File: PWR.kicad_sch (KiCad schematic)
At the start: 32 parts, among them J1 Conn_01x02_Pin, U2 XC6206P332MR, U4 MCP6001-OT, U5 AMS1117-3.3, U6 XL1509-5.0

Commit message: feat: начал работу над проектом пульта управления, продумана входная цепь питания устройства
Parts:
- removed C10, C11: 100u, Capacitor_SMD:C_Elec_6.3x7.7, symbol Device:C_Small_US
- removed C43, C44, C9: 0.1u, Capacitor_SMD:C_0805_2012Metric_Pad1.18x1.45mm_HandSolder, symbol Device:C_Small
- removed D1: SMAJ30CA, Diode_SMD:D_SMA, symbol Diode:SMAJ30CA
- removed D2, D3: SS36, Diode_SMD:D_SMA, symbol Diode:SS36
- removed J1: Conn_01x02_Pin, Connector_PinHeader_2.54mm:PinHeader_1x02_P2.54mm_Vertical, symbol Connector:Conn_01x02_Pin
- removed L4: 47uH, Inductor_SMD:L_12x12mm_H8mm, symbol Inductors:L
- removed L5: BLM21PG121SN1D, Inductor_SMD:L_0805_2012Metric_Pad1.05x1.20mm_HandSolder, symbol Inductors:L
- removed U6: XL1509-5.0, Package_SO:SOIC-8-1EP_3.9x4.9mm_P1.27mm_EP2.29x3mm_ThermalVias, symbol Power_suply:XL1509-5.0
- added C12: 100u, Capacitor_SMD:C_Elec_6.3x7.7, symbol Device:C_Small_US
- added D1: SS32, Diode_SMD:D_SMA, symbol Diode:SS32
- added D3: SMAJ5.0CA, Diode_SMD:D_SMA, symbol Diode:SMAJ5.0CA
- added J1: USB_B_Micro, Connector_USB:USB_Micro-B_Wuerth_629105150521, symbol Connector:USB_B_Micro
- R10: value 1k -> 10k
- R9: value 3k -> 10k
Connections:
- net +5V: now also C4.1, L3.2, C12.1
- net GND: now also C12.2, D3.1 (A1), J1.5 (GND)
- net at C34.1, L3.1: now also D1.1 (K)
- removed net +12V: C4.1, L3.2, R9.1
- net +12V_1: no longer names the net of F1.1 (A1)
- net +12V_1: now also J1.1 (VBUS)
- net +12V_in renamed +5V_in
- net +5V_in: now also D1.2 (A), D3.2 (A2)
- new net BAT+: R9.1
- new net Earth: J1.SH (Shield)
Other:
- moved on the sheet: C1, C2, C29, C3, C30, C34, C4, C5, C6, C7, C8, F1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

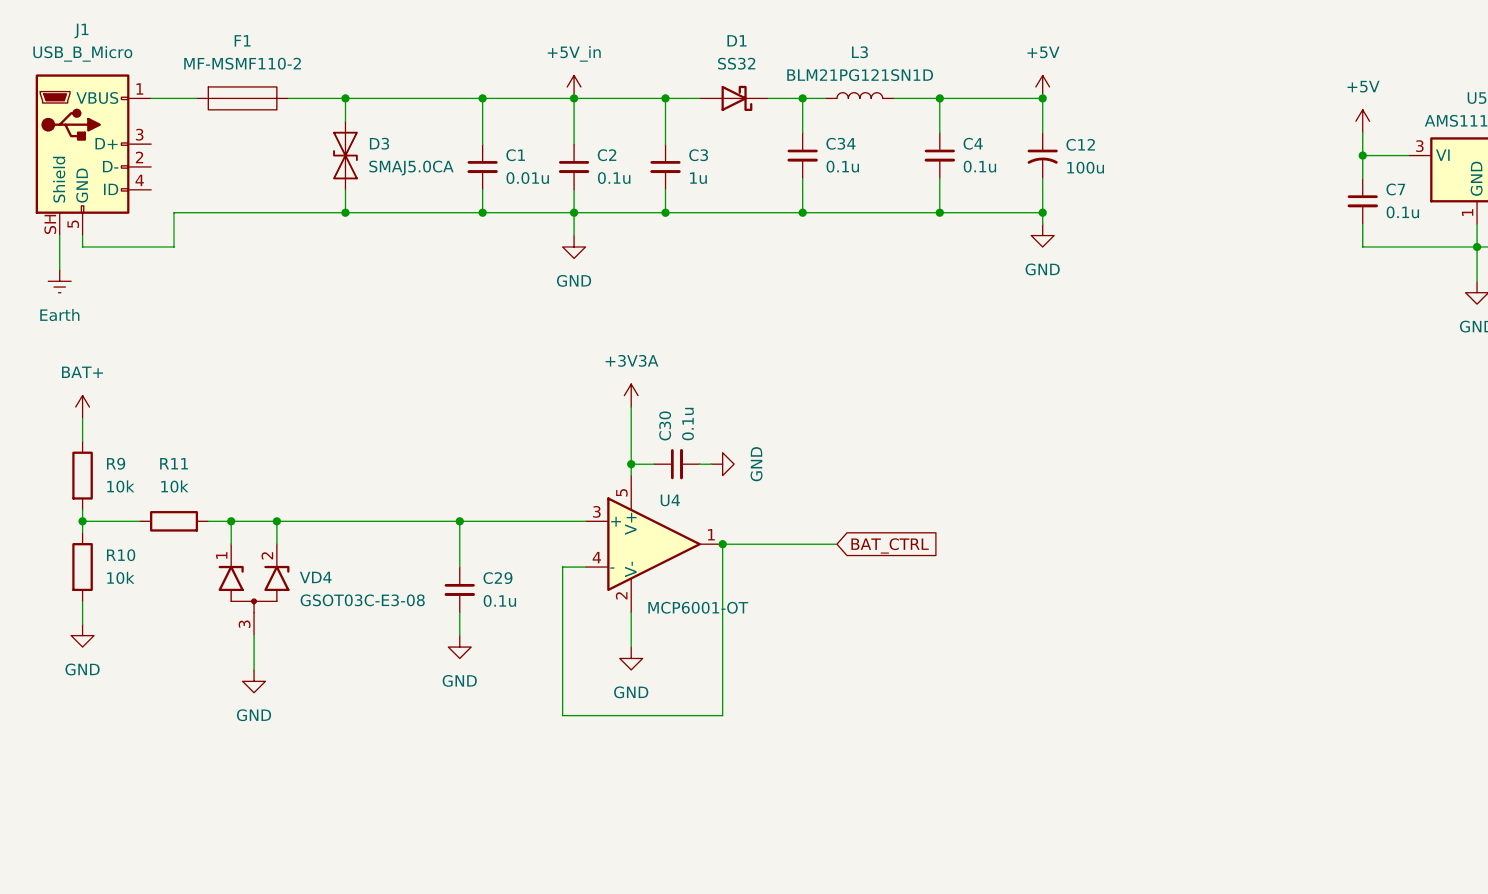
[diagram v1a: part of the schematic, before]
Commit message: feat: добавлен верный разъём USB
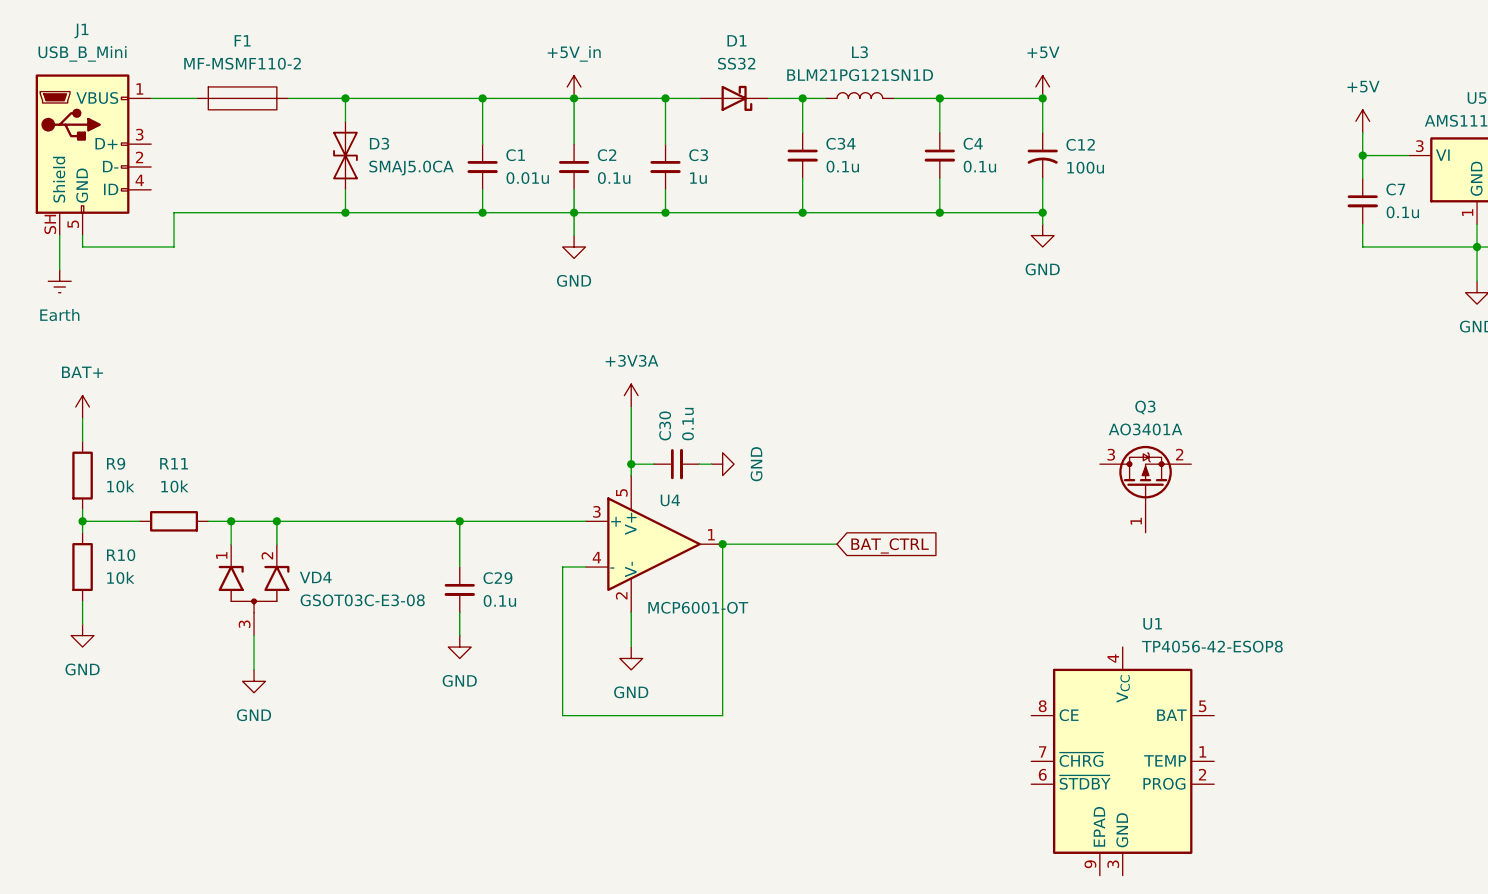
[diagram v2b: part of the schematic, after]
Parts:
- removed J1: USB_B_Micro, Connector_USB:USB_Micro-B_Wuerth_629105150521, symbol Connector:USB_B_Micro
- added J1: USB_B_Mini, Connector_USB:USB_Mini-B_Lumberg_2486_01_Horizontal, symbol Connector:USB_B_Mini
- added Q3: AO3401A, Package_TO_SOT_SMD:SOT-23, symbol Transistor_FET:AO3401A
- added U1: TP4056-42-ESOP8, Package_SO:SOIC-8-1EP_3.9x4.9mm_P1.27mm_EP2.41x3.3mm_ThermalVias, symbol Battery_Management:TP4056-42-ESOP8
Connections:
- net Earth: now also J1.SH (Shield)
- net GND: now also J1.5 (GND)
- net at F1.1 (A1): now also J1.1 (VBUS)
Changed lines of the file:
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@@
-	)
-	(symbol
-		(lib_id "Connector:USB_B_Micro")
-		(at 31.75 54.61 0)
-		(unit 1)
-		(body_style 1)
-		(exclude_from_sim no)
-		(in_bom yes)
-		(on_board yes)
-		(in_pos_files yes)
-		(dnp no)
-		(fields_autoplaced yes)
-		(property "Reference" "J1"
-			(at 31.75 41.91 0)
-			(show_name no)
-			(do_not_autoplace no)
-			(effects
-				(font
-					(size 1.27 1.27)
-				)
-			)
-		)
-		(property "Value" "USB_B_Micro"
-			(at 31.75 44.45 0)
-			(show_name no)
-			(do_not_autoplace no)
-			(effects
-				(font
-					(size 1.27 1.27)
-				)
-			)
-		)
-		(property "Footprint" "Connector_USB:USB_Micro-B_Wuerth_629105150521"
-			(at 35.56 55.88 0)
-			(hide yes)
-			(show_name no)
-			(do_not_autoplace no)
-			(effects
-				(font
-					(size 1.27 1.27)
-				)
-			)
-		)
-		(property "Datasheet" ""
-			(at 35.56 55.88 0)
-			(hide yes)
-			(show_name no)
-			(do_not_autoplace no)
-			(effects
-				(font
-					(size 1.27 1.27)
-				)
-			)
-		)
-		(property "Description" "USB Micro Type B connector"
-			(at 31.75 54.61 0)
-			(hide yes)
-			(show_name no)
-			(do_not_autoplace no)
-			(effects
-				(font
-					(size 1.27 1.27)
-				)
-			)
-		)
-		(pin "1"
-		)
-		(pin "3"
-		)
-		(pin "5"
-		)
-		(pin "2"
-		)
-		(pin "4"
-		)
-		(pin "SH"
-		)
-		(instances
-			(project "Magister_work_v1"
-				(path "/9ff4e5e8-ab59-4c4d-a10a-f8f5e444c5cb/6e6c00e0-c4a8-403b-83b3-c44ac9f0fdda"
-					(reference "J1")
-					(unit 1)
-				)
-			)
-		)
 	)
 	(symbol
@@
 	)
 	(symbol
+		(lib_id "Battery_Management:TP4056-42-ESOP8")
+		(at 147.32 123.19 0)
+		(unit 1)
+		(body_style 1)
+		(exclude_from_sim no)
+		(in_bom yes)
+		(on_board yes)
+		(in_pos_files yes)
+		(dnp no)
+		(fields_autoplaced yes)
+		(property "Reference" "U1"
+			(at 149.4633 107.95 0)
+			(show_name no)
+			(do_not_autoplace no)
+			(effects
+				(font
+					(size 1.27 1.27)
+				)
+				(justify left)
+			)
+		)
+		(property "Value" "TP4056-42-ESOP8"
+			(at 149.4633 110.49 0)
+			(show_name no)
+			(do_not_autoplace no)
+			(effects
+				(font
+					(size 1.27 1.27)
+				)
+				(justify left)
+			)
+		)
+		(property "Footprint" "Package_SO:SOIC-8-1EP_3.9x4.9mm_P1.27mm_EP2.41x3.3mm_ThermalVias"
+			(at 147.828 146.05 0)
+			(hide yes)
+			(show_name no)
+			(do_not_autoplace no)
+			(effects
+				(font
+					(size 1.27 1.27)
+				)
+			)
+		)
+		(property "Datasheet" "https://www.lcsc.com/datasheet/lcsc_datasheet_2410121619_TOPPOWER-Nanjing-Extension-Microelectronics-TP4056-42-ESOP8_C16581.pdf"
+			(at 147.32 148.59 0)
+			(hide yes)
+			(show_name no)
+			(do_not_autoplace no)
+			(effects
+				(font
+					(size 1.27 1.27)
+				)
+			)
+		)
+		(property "Description" "1A Standalone Linear Li-ion/LiPo single-cell battery charger, 4.2V ±1% charge voltage, VCC = 4.0..8.0V, SOIC-8 (SOP-8)"
+			(at 147.828 143.51 0)
+			(hide yes)
+			(show_name no)
+			(do_not_autoplace no)
+			(effects
+				(font
+					(size 1.27 1.27)
+				)
+			)
+		)
+		(pin "4"
+		)
+		(pin "2"
+		)
+		(pin "9"
+		)
+		(pin "1"
+		)
+		(pin "5"
+		)
+		(pin "6"
+		)
+		(pin "8"
+		)
+		(pin "7"
+		)
+		(pin "3"
+		)
+		(instances
+			(project "Magister_work_v1"
+				(path "/9ff4e5e8-ab59-4c4d-a10a-f8f5e444c5cb/6e6c00e0-c4a8-403b-83b3-c44ac9f0fdda"
+					(reference "U1")
+					(unit 1)
+				)
+			)
+		)
+	)
+	(symbol
 		(lib_id "power:GND")
 		(at 138.43 63.5 0)
@@
 	)
 	(symbol
+		(lib_id "Transistor_FET:AO3401A")
+		(at 149.86 92.71 90)
+		(unit 1)
+		(body_style 1)
+		(exclude_from_sim no)
+		(in_bom yes)
+		(on_board yes)
+		(in_pos_files yes)
+		(dnp no)
+		(fields_autoplaced yes)
+		(property "Reference" "Q3"
+			(at 149.86 83.82 90)
+			(show_name no)
+			(do_not_autoplace no)
+			(effects
+				(font
+					(size 1.27 1.27)
+				)
+			)
+		)
+		(property "Value" "AO3401A"
+			(at 149.86 86.36 90)
+			(show_name no)
+			(do_not_autoplace no)
+			(effects
+				(font
+					(size 1.27 1.27)
+				)
+			)
+		)
+		(property "Footprint" "Package_TO_SOT_SMD:SOT-23"
+			(at 151.765 87.63 0)
+			(hide yes)
+			(show_name no)
+			(do_not_autoplace no)
+			(effects
+				(font
+					(size 1.27 1.27)
+					(italic yes)
+				)
+				(justify left)
+			)
+		)
+		(property "Datasheet" "http://www.aosmd.com/pdfs/datasheet/AO3401A.pdf"
+			(at 153.67 87.63 0)
+			(hide yes)
+			(show_name no)
+			(do_not_autoplace no)
+			(effects
+				(font
+					(size 1.27 1.27)
+				)
+				(justify left)
+			)
+		)
+		(property "Description" "-4.0A Id, -30V Vds, P-Channel MOSFET, SOT-23"
+			(at 149.86 92.71 0)
+			(hide yes)
+			(show_name no)
+			(do_not_autoplace no)
+			(effects
+				(font
+					(size 1.27 1.27)
+				)
+			)
+		)
+		(pin "1"
+		)
+		(pin "3"
+		)
+		(pin "2"
+		)
+		(instances
+			(project "Magister_work_v1"
+				(path "/9ff4e5e8-ab59-4c4d-a10a-f8f5e444c5cb/6e6c00e0-c4a8-403b-83b3-c44ac9f0fdda"
+					(reference "Q3")
+					(unit 1)
+				)
+			)
+		)
+	)
+	(symbol
 		(lib_id "Power_suply:XC6206P332MR")
 		(at 227.33 52.07 0)
@@
 					(unit 1)
 				)
+			)
+		)
+	)
+	(symbol
+		(lib_id "Connector:USB_B_Mini")
+		(at 31.75 54.61 0)
+		(unit 1)
+		(body_style 1)
+		(exclude_from_sim no)
+		(in_bom yes)
+		(on_board yes)
+		(in_pos_files yes)
+		(dnp no)
+		(fields_autoplaced yes)
+		(property "Reference" "J1"
+			(at 31.75 41.91 0)
+			(show_name no)
+			(do_not_autoplace no)
+			(effects
+				(font
+					(size 1.27 1.27)
+				)
+			)
+		)
+		(property "Value" "USB_B_Mini"
+			(at 31.75 44.45 0)
+			(show_name no)
+			(do_not_autoplace no)
+			(effects
+				(font
+					(size 1.27 1.27)
+				)
+			)
+		)
+		(property "Footprint" "Connector_USB:USB_Mini-B_Lumberg_2486_01_Horizontal"
+			(at 35.56 55.88 0)
+			(hide yes)
+			(show_name no)
+			(do_not_autoplace no)
+			(effects
+				(font
+					(size 1.27 1.27)
+				)
+			)
+		)
+		(property "Datasheet" ""
+			(at 35.56 55.88 0)
+			(hide yes)
+			(show_name no)
+			(do_not_autoplace no)
+			(effects
+				(font
+					(size 1.27 1.27)
+				)
+			)
+		)
+		(property "Description" "USB Mini Type B connector"
+			(at 31.75 54.61 0)
+			(hide yes)
+			(show_name no)
+			(do_not_autoplace no)
+			(effects
+				(font
+					(size 1.27 1.27)
+				)
+			)
+		)
+		(pin "5"
+		)
+		(pin "4"
+		)
+		(pin "SH"
+		)
+		(pin "1"
+		)
+		(pin "2"
+		)
+		(pin "3"
+		)
+		(instances
+			(project "Magister_work_v1"
+				(path "/9ff4e5e8-ab59-4c4d-a10a-f8f5e444c5cb/6e6c00e0-c4a8-403b-83b3-c44ac9f0fdda"
+					(reference "J1")
+					(unit 1)
+				)

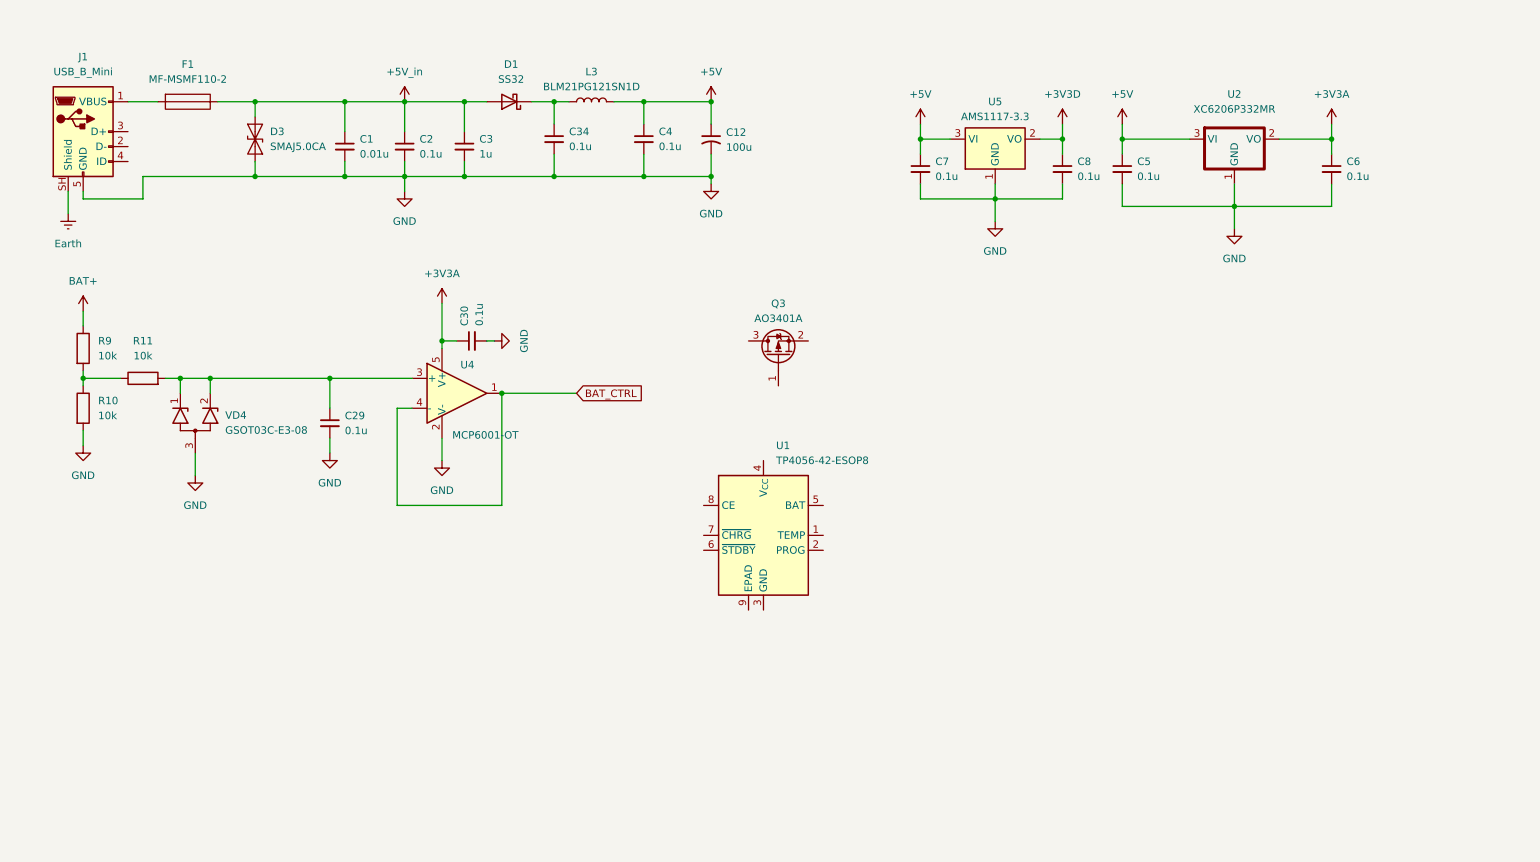
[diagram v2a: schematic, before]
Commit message: feat: добавлена цепь питания и заряда батареи для аварийного питания
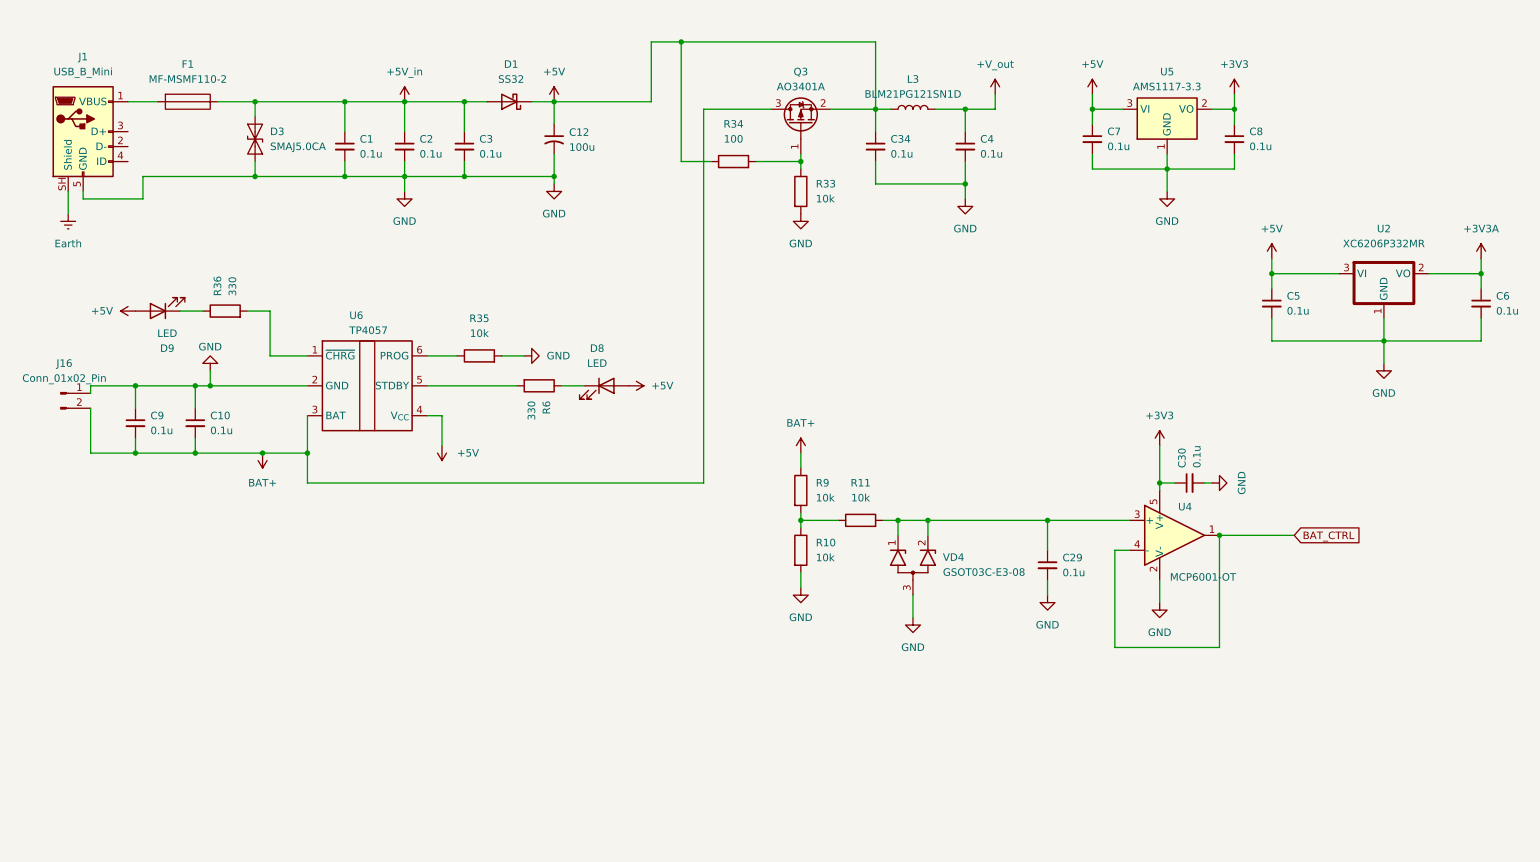
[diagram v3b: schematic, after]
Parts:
- removed U1: TP4056-42-ESOP8, Package_SO:SOIC-8-1EP_3.9x4.9mm_P1.27mm_EP2.41x3.3mm_ThermalVias, symbol Battery_Management:TP4056-42-ESOP8
- added C10, C9: 0.1u, Capacitor_SMD:C_0805_2012Metric_Pad1.18x1.45mm_HandSolder, symbol Device:C_Small
- added D8, D9: LED, LED_SMD:LED_0805_2012Metric_Pad1.15x1.40mm_HandSolder, symbol Device:LED
- added J16: Conn_01x02_Pin, Connector_Hirose:Hirose_DF13-02P-1.25DSA_1x02_P1.25mm_Vertical, symbol Connector:Conn_01x02_Pin
- added R33, R35: 10k, Resistor_SMD:R_0805_2012Metric_Pad1.20x1.40mm_HandSolder, symbol Device:R
- added R34: 100, Resistor_SMD:R_0805_2012Metric_Pad1.20x1.40mm_HandSolder, symbol Device:R
- added R36, R6: 330, Resistor_SMD:R_0805_2012Metric_Pad1.20x1.40mm_HandSolder, symbol Device:R
- added U6: TP4057, Package_TO_SOT_SMD:TSOT-23-6, symbol Battery_Management:TP4057
- C1: value 0.01u -> 0.1u
- C3: value 1u -> 0.1u
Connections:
- net +3V3A: no longer C30.1, U4.5 (V+)
- net +5V: now also C34.1, D1.1 (K), L3.1, Q3.2 (S), D8.2 (A), D9.2 (A), R34.1, U6.4 (V_{CC}); no longer C4.1, L3.2
- net BAT+: now also Q3.3 (D), C10.2, C9.2, J16.2 (Pin_2), U6.3 (BAT)
- net GND: now also C10.1, C9.1, J16.1 (Pin_1), R33.2, R35.2, U6.2 (GND)
- net at Q3.1 (G): now also R33.1, R34.2
- net +3V3D renamed +3V3
- net +3V3: now also C30.1, U4.5 (V+)
- new net: D8.1 (K), R6.1
- new net: D9.1 (K), R36.1
- new net: R35.1, U6.6 (PROG)
- new net: R6.2, U6.5 (STDBY)
- new net: R36.2, U6.1 (~{CHRG})
- new net +V_out: C4.1, L3.2
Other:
- moved on the sheet: C12, C29, C30, C5, C6, C7, C8, Q3, R10, R11, R9, U2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
